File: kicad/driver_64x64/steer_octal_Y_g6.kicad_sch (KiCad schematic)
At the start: 66 parts

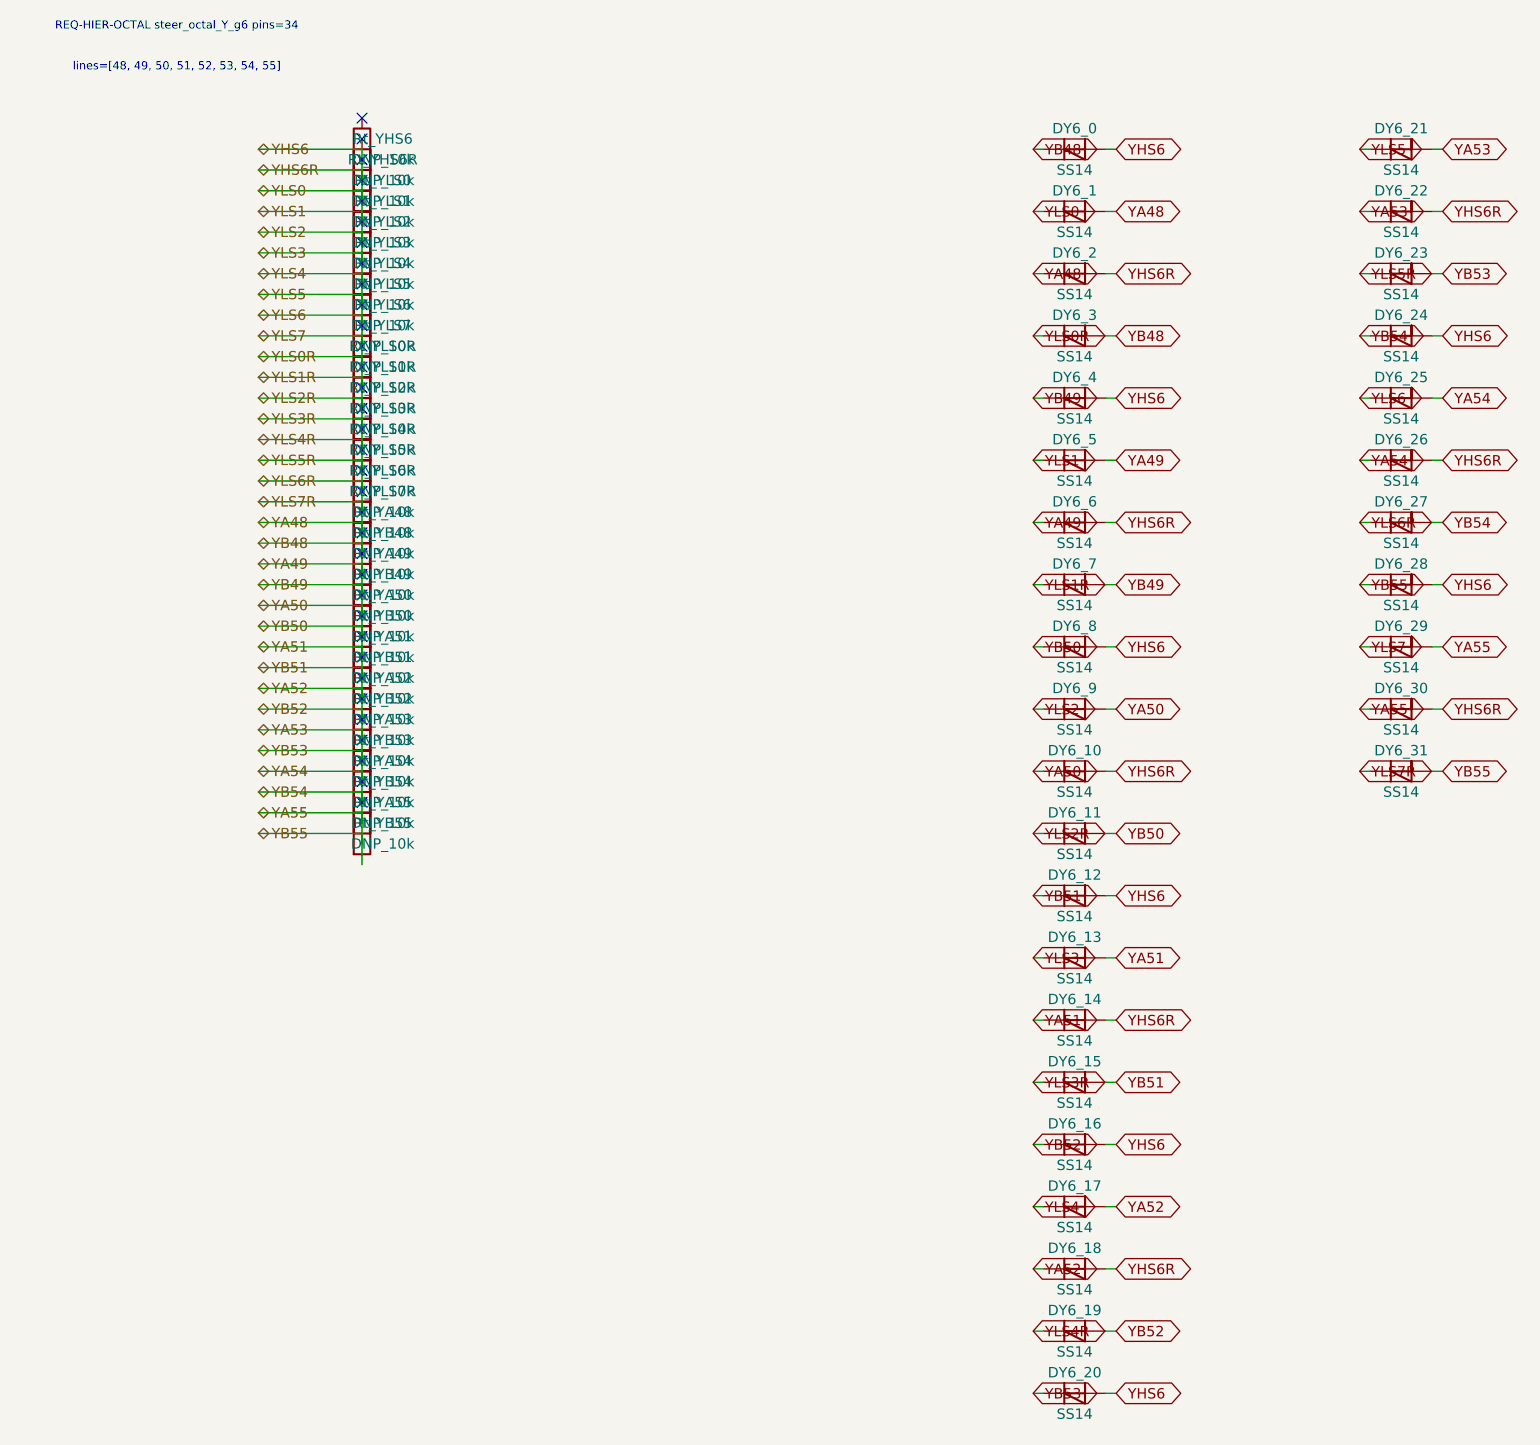
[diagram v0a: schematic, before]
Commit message: logical seperation into host and multiple decode/drive/steering boards
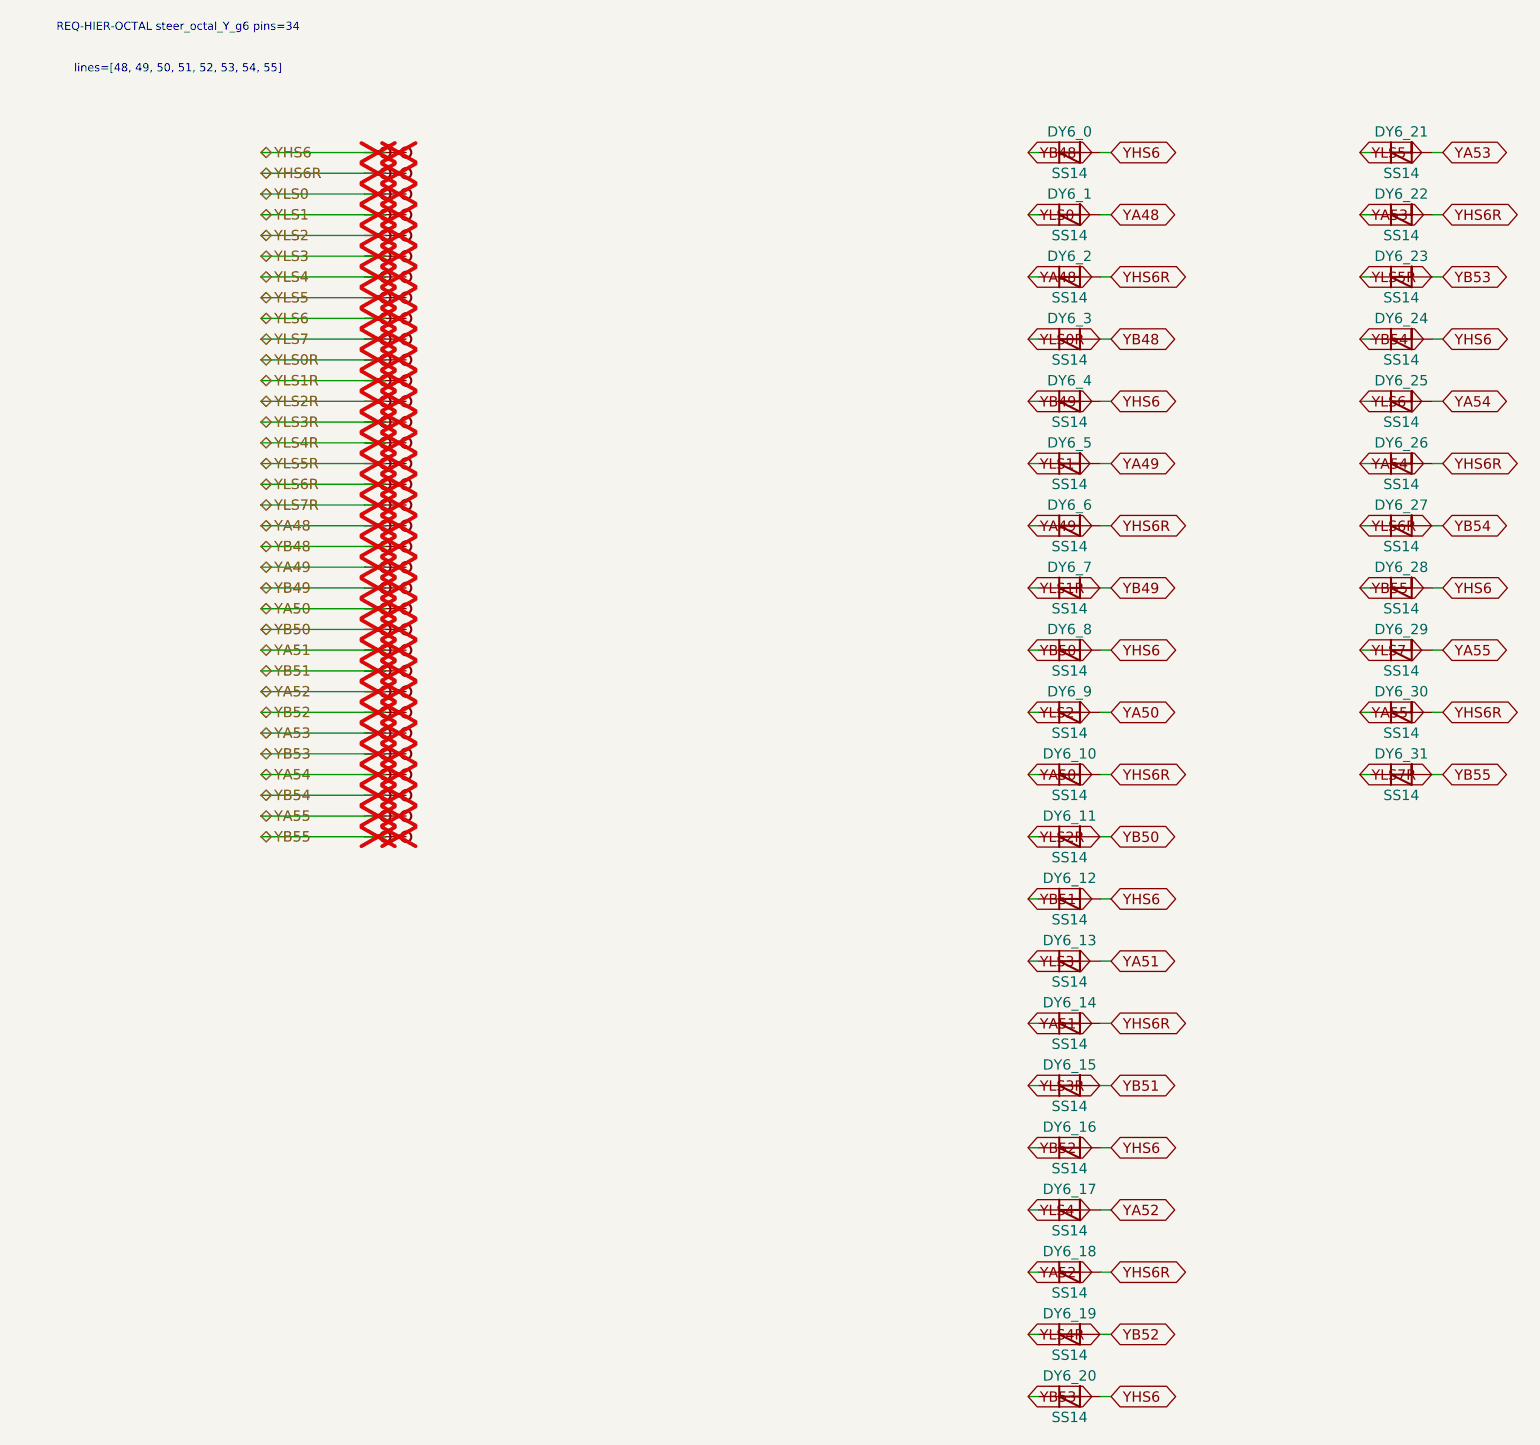
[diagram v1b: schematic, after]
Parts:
- removed Rt_YA48, Rt_YA49, Rt_YA50, Rt_YA51, Rt_YA52, Rt_YA53, Rt_YA54, Rt_YA55, Rt_YB48, Rt_YB49, Rt_YB50, Rt_YB51, Rt_YB52, Rt_YB53, Rt_YB54, Rt_YB55, Rt_YHS6, Rt_YHS6R, Rt_YLS0, Rt_YLS0R, Rt_YLS1, Rt_YLS1R, Rt_YLS2, Rt_YLS2R, Rt_YLS3, Rt_YLS3R, Rt_YLS4, Rt_YLS4R, Rt_YLS5, Rt_YLS5R, Rt_YLS6, Rt_YLS6R, Rt_YLS7, Rt_YLS7R: DNP_10k, symbol Device:R
- added TP_YA48, TP_YA48b, TP_YA49, TP_YA49b, TP_YA50, TP_YA50b, TP_YA51, TP_YA51b, TP_YA52, TP_YA52b, TP_YA53, TP_YA53b, TP_YA54, TP_YA54b, TP_YA55, TP_YA55b, TP_YB48, TP_YB48b, TP_YB49, TP_YB49b, TP_YB50, TP_YB50b, TP_YB51, TP_YB51b, TP_YB52, TP_YB52b, TP_YB53, TP_YB53b, TP_YB54, TP_YB54b, TP_YB55, TP_YB55b, TP_YHS6, TP_YHS6R, TP_YHS6Rb, TP_YHS6b, TP_YLS0, TP_YLS0R, TP_YLS0Rb, TP_YLS0b, TP_YLS1, TP_YLS1R, TP_YLS1Rb, TP_YLS1b, TP_YLS2, TP_YLS2R, TP_YLS2Rb, TP_YLS2b, TP_YLS3, TP_YLS3R, TP_YLS3Rb, TP_YLS3b, TP_YLS4, TP_YLS4R, TP_YLS4Rb, TP_YLS4b, TP_YLS5, TP_YLS5R, TP_YLS5Rb, TP_YLS5b, TP_YLS6, TP_YLS6R, TP_YLS6Rb, TP_YLS6b, TP_YLS7, TP_YLS7R, TP_YLS7Rb, TP_YLS7b: Stub, symbol CMR:Stub
- DY6_0, DY6_1, DY6_10, DY6_11, DY6_12, DY6_13, DY6_14, DY6_15, DY6_16, DY6_17, DY6_18, DY6_19, DY6_2, DY6_20, DY6_21, DY6_22, DY6_23, DY6_24, DY6_25, DY6_26, DY6_27, DY6_28, DY6_29, DY6_3, DY6_30, DY6_31, DY6_4, DY6_5, DY6_6, DY6_7, DY6_8, DY6_9: symbol Device:D_Schottky -> CMR:D_Schottky
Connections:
- net YA48: now also TP_YA48.1, TP_YA48b.1; no longer DY6_0.1 (K), DY6_0.2 (A), DY6_1.1 (K), DY6_10.1 (K), DY6_10.2 (A), DY6_11.1 (K), DY6_11.2 (A), DY6_12.1 (K), DY6_12.2 (A), DY6_13.1 (K), DY6_13.2 (A), DY6_14.1 (K), DY6_14.2 (A), DY6_15.1 (K), DY6_15.2 (A), DY6_16.1 (K), DY6_16.2 (A), DY6_17.1 (K), DY6_17.2 (A), DY6_18.1 (K), DY6_18.2 (A), DY6_19.1 (K), DY6_19.2 (A), DY6_2.2 (A), DY6_20.1 (K), DY6_20.2 (A), DY6_21.1 (K), DY6_21.2 (A), DY6_22.1 (K), DY6_22.2 (A), DY6_23.1 (K), DY6_23.2 (A), DY6_24.1 (K), DY6_24.2 (A), DY6_25.1 (K), DY6_25.2 (A), DY6_26.1 (K), DY6_26.2 (A), DY6_27.1 (K), DY6_27.2 (A), DY6_28.1 (K), DY6_28.2 (A), DY6_29.1 (K), DY6_29.2 (A), DY6_3.1 (K), DY6_3.2 (A), DY6_30.1 (K), DY6_30.2 (A), DY6_31.1 (K), DY6_31.2 (A), DY6_4.1 (K), DY6_4.2 (A), DY6_5.1 (K), DY6_5.2 (A), DY6_6.1 (K), DY6_6.2 (A), DY6_7.1 (K), DY6_7.2 (A), DY6_8.1 (K), DY6_8.2 (A), DY6_9.1 (K), DY6_9.2 (A)
- new net YA49: DY6_5.2 (A), DY6_6.1 (K), TP_YA49.1, TP_YA49b.1
- new net YA50: DY6_10.1 (K), DY6_9.2 (A), TP_YA50.1, TP_YA50b.1
- new net YA51: DY6_13.2 (A), DY6_14.1 (K), TP_YA51.1, TP_YA51b.1
- new net YA52: DY6_17.2 (A), DY6_18.1 (K), TP_YA52.1, TP_YA52b.1
- new net YA53: DY6_21.2 (A), DY6_22.1 (K), TP_YA53.1, TP_YA53b.1
- new net YA54: DY6_25.2 (A), DY6_26.1 (K), TP_YA54.1, TP_YA54b.1
- new net YA55: DY6_29.2 (A), DY6_30.1 (K), TP_YA55.1, TP_YA55b.1
- new net YB48: DY6_0.1 (K), DY6_3.2 (A), TP_YB48.1, TP_YB48b.1
- new net YB49: DY6_4.1 (K), DY6_7.2 (A), TP_YB49.1, TP_YB49b.1
- new net YB50: DY6_11.2 (A), DY6_8.1 (K), TP_YB50.1, TP_YB50b.1
- new net YB51: DY6_12.1 (K), DY6_15.2 (A), TP_YB51.1, TP_YB51b.1
- new net YB52: DY6_16.1 (K), DY6_19.2 (A), TP_YB52.1, TP_YB52b.1
- new net YB53: DY6_20.1 (K), DY6_23.2 (A), TP_YB53.1, TP_YB53b.1
- new net YB54: DY6_24.1 (K), DY6_27.2 (A), TP_YB54.1, TP_YB54b.1
- new net YB55: DY6_28.1 (K), DY6_31.2 (A), TP_YB55.1, TP_YB55b.1
- new net YHS6: DY6_0.2 (A), DY6_12.2 (A), DY6_16.2 (A), DY6_20.2 (A), DY6_24.2 (A), DY6_28.2 (A), DY6_4.2 (A), DY6_8.2 (A), TP_YHS6.1, TP_YHS6b.1
- new net YHS6R: DY6_10.2 (A), DY6_14.2 (A), DY6_18.2 (A), DY6_2.2 (A), DY6_22.2 (A), DY6_26.2 (A), DY6_30.2 (A), DY6_6.2 (A), TP_YHS6R.1, TP_YHS6Rb.1
- new net YLS0: DY6_1.1 (K), TP_YLS0.1, TP_YLS0b.1
- new net YLS0R: DY6_3.1 (K), TP_YLS0R.1, TP_YLS0Rb.1
- new net YLS1: DY6_5.1 (K), TP_YLS1.1, TP_YLS1b.1
- new net YLS1R: DY6_7.1 (K), TP_YLS1R.1, TP_YLS1Rb.1
- new net YLS2: DY6_9.1 (K), TP_YLS2.1, TP_YLS2b.1
- new net YLS2R: DY6_11.1 (K), TP_YLS2R.1, TP_YLS2Rb.1
- new net YLS3: DY6_13.1 (K), TP_YLS3.1, TP_YLS3b.1
- new net YLS3R: DY6_15.1 (K), TP_YLS3R.1, TP_YLS3Rb.1
- new net YLS4: DY6_17.1 (K), TP_YLS4.1, TP_YLS4b.1
- new net YLS4R: DY6_19.1 (K), TP_YLS4R.1, TP_YLS4Rb.1
- new net YLS5: DY6_21.1 (K), TP_YLS5.1, TP_YLS5b.1
- new net YLS5R: DY6_23.1 (K), TP_YLS5R.1, TP_YLS5Rb.1
- new net YLS6: DY6_25.1 (K), TP_YLS6.1, TP_YLS6b.1
- new net YLS6R: DY6_27.1 (K), TP_YLS6R.1, TP_YLS6Rb.1
- new net YLS7: DY6_29.1 (K), TP_YLS7.1, TP_YLS7b.1
- new net YLS7R: DY6_31.1 (K), TP_YLS7R.1, TP_YLS7Rb.1
- no-connect marks 34 -> 0
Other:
- moved on the sheet: DY6_0, DY6_1, DY6_10, DY6_11, DY6_12, DY6_13, DY6_14, DY6_15, DY6_16, DY6_17, DY6_18, DY6_19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
